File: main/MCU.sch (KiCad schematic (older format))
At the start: 22 parts, among them J10 MCU_debug, J11 MCU_GPIO, J12 Conn_02x04_Odd_Even, U5 EFM32GG12B810F1024GQ64, X2 MCU Oscillator (72MHZ)

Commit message: Fix up after review 3
Add +3.3V and GND to MCU and FPGA GPIO.

Add a lot of footprints.
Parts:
- removed J11: MCU_GPIO, symbol Connector_Generic:Conn_02x05_Counter_Clockwise
- added J5: MCU_GPIO, symbol Connector_Generic:Conn_02x06_Odd_Even
- J12: value Conn_02x04_Odd_Even -> BACKUP_SPI
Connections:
- wire segments 177 -> 181
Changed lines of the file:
@@
 $Descr A4 11693 8268
 encoding utf-8
-Sheet 7 7
+Sheet 6 7
 Title "MIDI Audio Box"
 Date "2021-09-21"
@@
 Text Notes 3950 6850 0    50   ~ 10
 Decoupling capacitors (see AN0002.1, page 13)
-$Comp
-L Connector_Generic:Conn_02x05_Counter_Clockwise J11
-U 1 1 6149651E
-P 1500 4800
-F 0 "J11" H 1550 5217 50  0000 C CNN
-F 1 "MCU_GPIO" H 1550 5126 50  0000 C CNN
-F 2 "" H 1500 4800 50  0001 C CNN
-F 3 "~" H 1500 4800 50  0001 C CNN
-	1    1500 4800
-	1    0    0    -1
-$EndComp
 Wire Bus Line
-	900  5150 2200 5150
+	900  5700 2200 5700
 Wire Bus Line
 	2200 4450 4150 4450
@@
 P 1100 6500
 F 0 "J12" H 1150 6075 50  0000 C CNN
-F 1 "Conn_02x04_Odd_Even" H 1150 6166 50  0000 C CNN
+F 1 "BACKUP_SPI" H 1150 6166 50  0000 C CNN
 F 2 "" H 1100 6500 50  0001 C CNN
 F 3 "~" H 1100 6500 50  0001 C CNN
@@
 High Frequency Oscillator
 NoConn ~ 4650 4950
+$Comp
+L Connector_Generic:Conn_02x06_Odd_Even J5
+U 1 1 61CACD05
+P 1500 4800
+F 0 "J5" H 1550 5217 50  0000 C CNN
+F 1 "MCU_GPIO" H 1550 5126 50  0000 C CNN
+F 2 "" H 1500 4800 50  0001 C CNN
+F 3 "~" H 1500 4800 50  0001 C CNN
+	1    1500 4800
+	1    0    0    -1
+$EndComp
+$Comp
+L power:+3.3V #PWR076
+U 1 1 61CC3716
+P 1200 5250
+F 0 "#PWR076" H 1200 5100 50  0001 C CNN
+F 1 "+3.3V" H 1215 5423 50  0000 C CNN
+F 2 "" H 1200 5250 50  0001 C CNN
+F 3 "" H 1200 5250 50  0001 C CNN
+	1    1200 5250
+	-1   0    0    1
+$EndComp
+Wire Wire Line
+	1200 5250 1200 5100
+Wire Wire Line
+	1200 5100 1300 5100
+$Comp
+L power:GND #PWR077
+U 1 1 61CCF946
+P 1950 5300
+F 0 "#PWR077" H 1950 5050 50  0001 C CNN
+F 1 "GND" H 1955 5127 50  0000 C CNN
+F 2 "" H 1950 5300 50  0001 C CNN
+F 3 "" H 1950 5300 50  0001 C CNN
+	1    1950 5300
+	1    0    0    -1
+$EndComp
+Wire Wire Line
+	1950 5300 1950 5100
+Wire Wire Line
+	1950 5100 1800 5100
 Wire Bus Line
 	5250 950  5250 1650
 Wire Bus Line
-	2200 4450 2200 5150
+	2200 4450 2200 5700
 Wire Bus Line
-	900  4700 900  5150
+	900  4700 900  5700
 Wire Bus Line
 	4150 3450 4150 4450

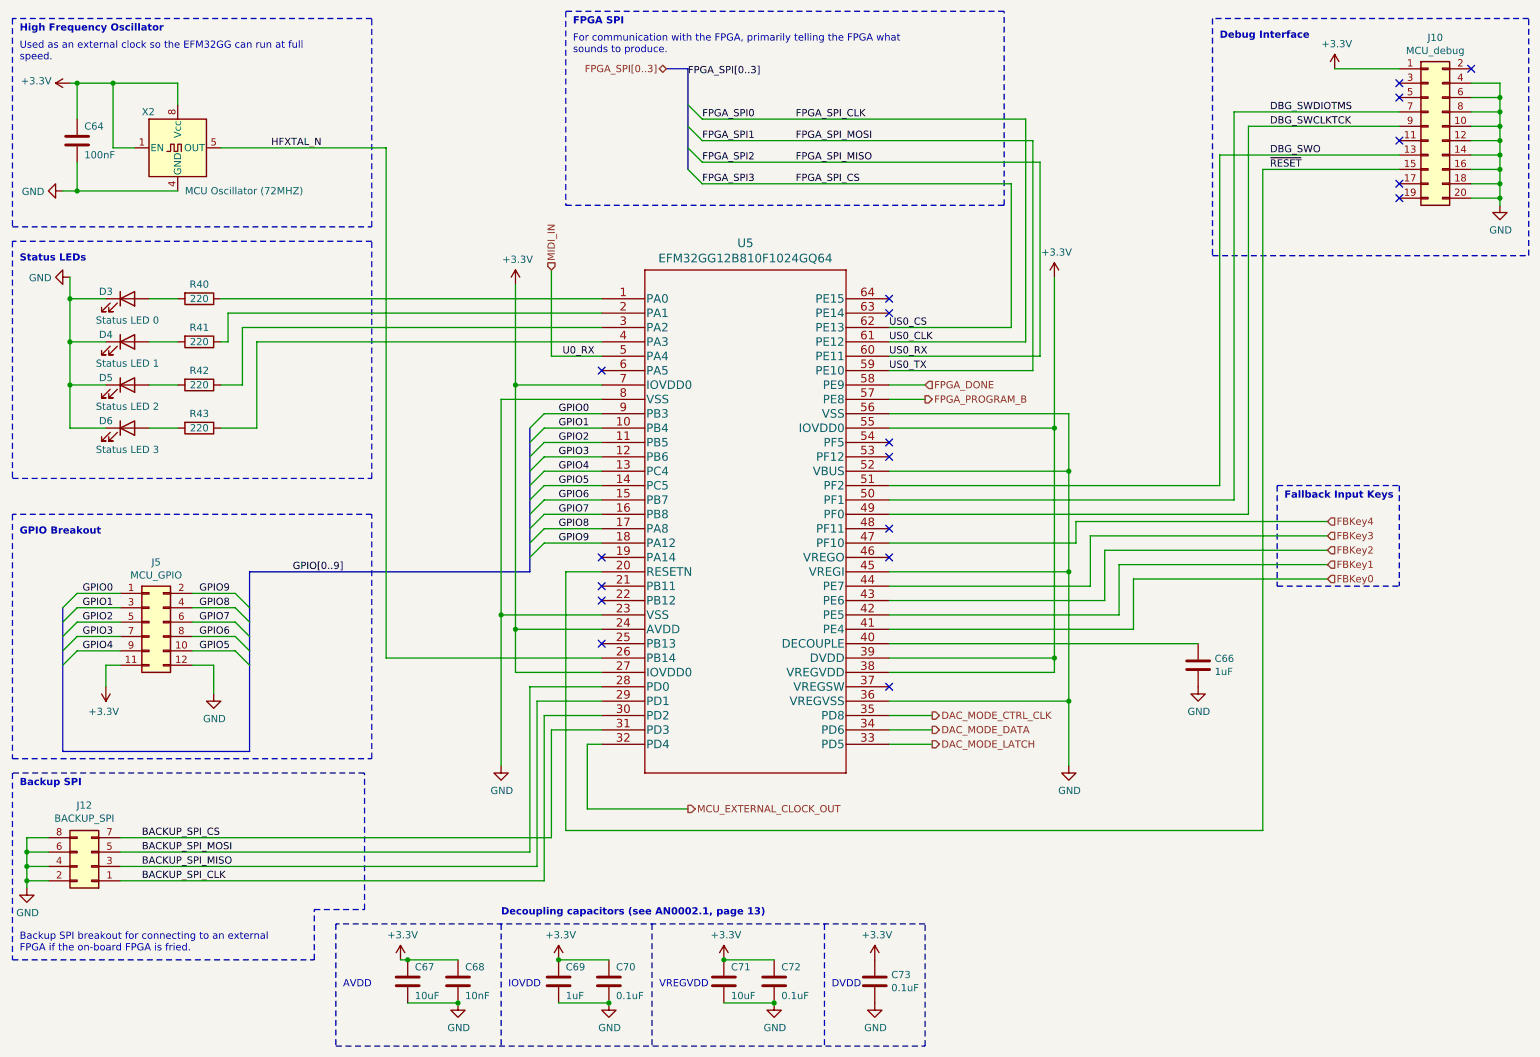
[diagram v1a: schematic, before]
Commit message: DAC: Remove amplifier, replace with low pass as per datasheet
Also: a lot of footprint association
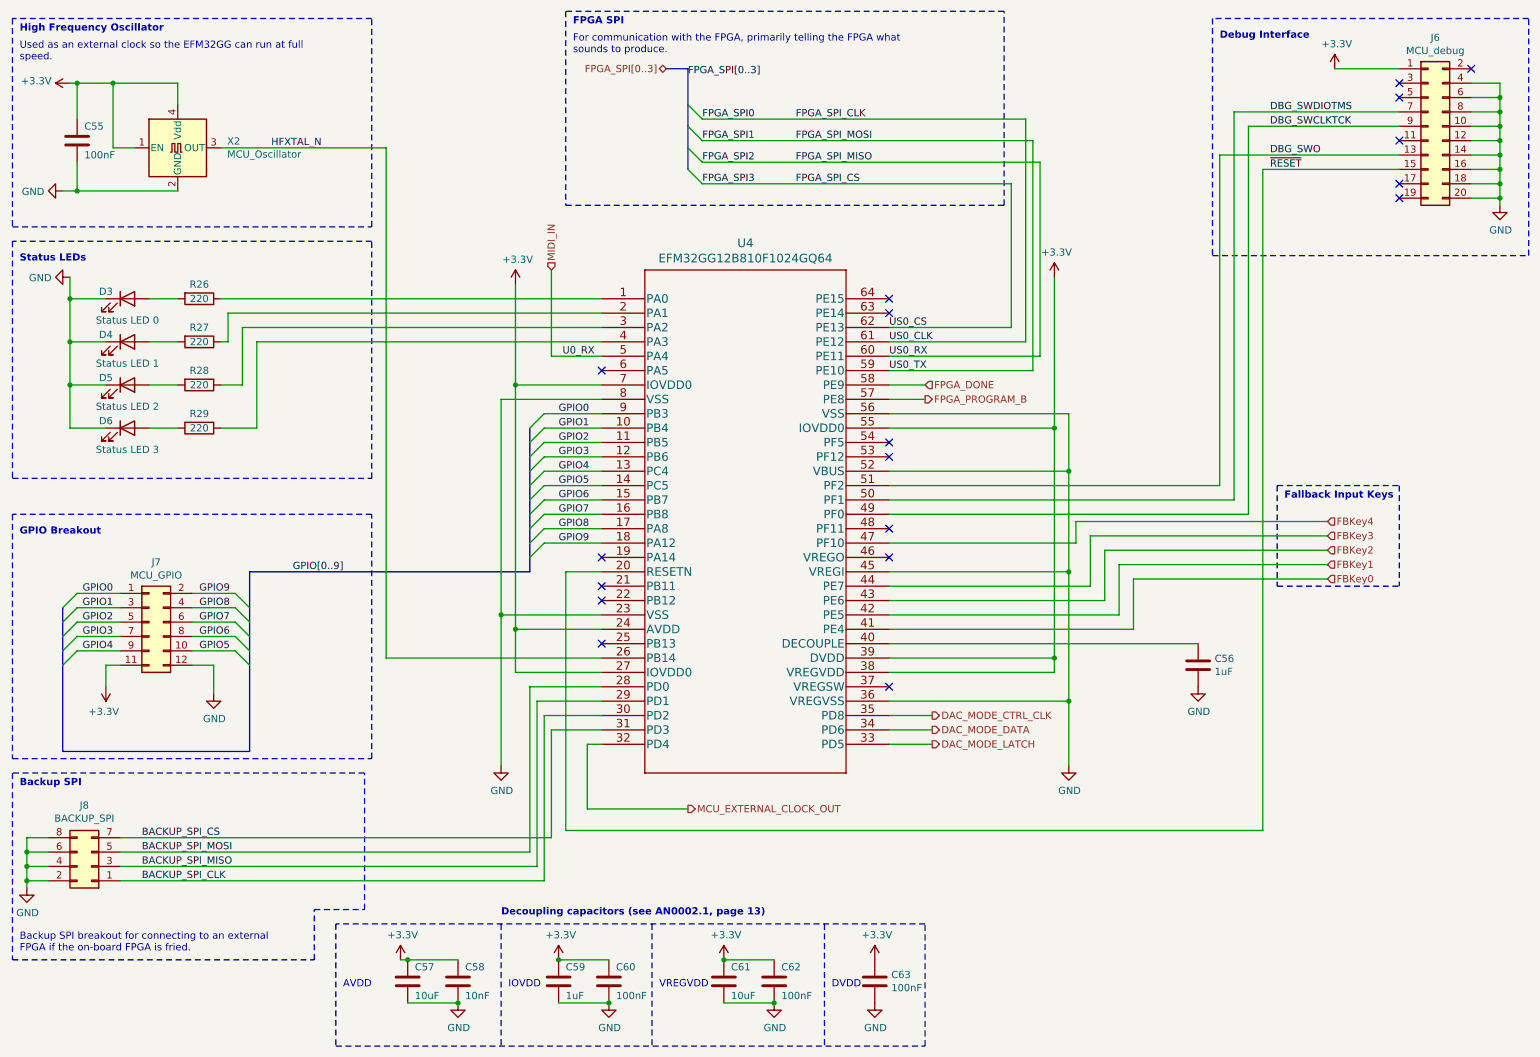
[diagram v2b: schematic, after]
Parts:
- removed X2: MCU Oscillator (72MHZ), Oscillator:Oscillator_DIP-8, symbol Oscillator:CXO_DIP8
- added X2: MCU_Oscillator, symbol Oscillator:TXC-7C
- C55: renamed from C64; footprint (none) -> Capacitor_SMD:C_0805_2012Metric_Pad1.18x1.45mm_HandSolder
- C56: renamed from C66; footprint (none) -> Capacitor_SMD:C_0805_2012Metric_Pad1.18x1.45mm_HandSolder
- C57: renamed from C67; footprint (none) -> Capacitor_SMD:C_0805_2012Metric_Pad1.18x1.45mm_HandSolder
- C58: renamed from C68; footprint (none) -> Capacitor_SMD:C_0805_2012Metric_Pad1.18x1.45mm_HandSolder
- C59: renamed from C69; footprint (none) -> Capacitor_SMD:C_0805_2012Metric_Pad1.18x1.45mm_HandSolder
- C60: renamed from C70; value 0.1uF -> 100nF; footprint (none) -> Capacitor_SMD:C_0805_2012Metric_Pad1.18x1.45mm_HandSolder
- C61: renamed from C71; footprint (none) -> Capacitor_SMD:C_0805_2012Metric_Pad1.18x1.45mm_HandSolder
- C62: renamed from C72; value 0.1uF -> 100nF; footprint (none) -> Capacitor_SMD:C_0805_2012Metric_Pad1.18x1.45mm_HandSolder
- C63: renamed from C73; value 0.1uF -> 100nF; footprint (none) -> Capacitor_SMD:C_0805_2012Metric_Pad1.18x1.45mm_HandSolder
- J6: renamed from J10; footprint (none) -> Connector_PinHeader_1.27mm:PinHeader_2x10_P1.27mm_Vertical
- J7: renamed from J5; footprint (none) -> Connector_PinHeader_2.54mm:PinHeader_2x06_P2.54mm_Vertical
- J8: renamed from J12; footprint (none) -> Connector_PinHeader_2.54mm:PinHeader_2x04_P2.54mm_Vertical
- renumbered R40 to R26, R41 to R27, R42 to R28, R43 to R29, U5 to U4
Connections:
- net +3V3: now also X2.1 (EN), X2.4 (Vdd)
- net GND: now also X2.2 (GND)
- net HFXTAL_N: now also X2.3 (OUT)

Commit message: Start PCB layout
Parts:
- D3: value Status LED 0 -> Status LED; Manufacturer_Name (none) -> Wurth Electronic; Manufacturer_Part_Number (none) -> 150080RS75000; URL (none) -> https://no.farnell.com/wurth-elektronik/150080rs75000/led-0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
- D4: value Status LED 1 -> Status LED; Manufacturer_Name (none) -> Wurth Electronic; Manufacturer_Part_Number (none) -> 150080RS75000; URL (none) -> https://no.farnell.com/wurth-elektronik/150080rs75000/led-0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
- D5: value Status LED 2 -> Status LED; Manufacturer_Name (none) -> Wurth Electronic; Manufacturer_Part_Number (none) -> 150080RS75000; URL (none) -> https://no.farnell.com/wurth-elektronik/150080rs75000/led-0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
- D6: value Status LED 3 -> Status LED; Manufacturer_Name (none) -> Wurth Electronic; Manufacturer_Part_Number (none) -> 150080RS75000; URL (none) -> https://no.farnell.com/wurth-elektronik/150080rs75000/led-0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
- J7, J8: Comment (none) -> Same as FPGA_GPIO (Cut to length)
- U4: Manufacturer_Name (none) -> Silicon Labs; Manufacturer_Part_Number (none) -> EFM32GG12B810F1024GQ64-A; URL (none) -> https://no.farnell.com/silicon-labs/efm32gg12b810f1024gq64-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
- X2: footprint (none) -> Oscillator:Oscillator_SMD_SeikoEpson_SG210-4Pin_2.5x2.0mm_HandSoldering
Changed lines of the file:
@@
 F 1 "EFM32GG12B810F1024GQ64" H 5650 2831 60  0000 C CNN
 F 2 "EFM32GG12B810F1024Q64:EFM32GG12B810F1024GQ64" H 5650 2790 60  0001 C CNN
-F 3 "" H 4650 2550 60  0000 C CNN
+F 3 "https://www.farnell.com/datasheets/2719978.pdf" H 4650 2550 60  0000 C CNN
+F 4 "Silicon Labs" H 4650 2550 50  0001 C CNN "Manufacturer_Name"
+F 5 "EFM32GG12B810F1024GQ64-A" H 4650 2550 50  0001 C CNN "Manufacturer_Part_Number"
+F 6 "https://no.farnell.com/silicon-labs/efm32gg12b810f1024gq64-a/mcu-32bit-72mhz-qfp-64/dp/2950057" H 4650 2550 50  0001 C CNN "URL"
 	1    4650 2550
 	1    0    0    -1
@@
 P 1350 3450
 F 0 "D6" H 1200 3500 50  0000 C CNN
-F 1 "Status LED 3" H 1350 3300 50  0000 C CNN
+F 1 "Status LED" H 1350 3300 50  0000 C CNN
 F 2 "LED_SMD:LED_0805_2012Metric_Pad1.15x1.40mm_HandSolder" H 1350 3450 50  0001 C CNN
-F 3 "~" H 1350 3450 50  0001 C CNN
+F 3 "https://www.farnell.com/datasheets/1911350.pdf" H 1350 3450 50  0001 C CNN
+F 4 "Wurth Electronic" H 1350 3450 50  0001 C CNN "Manufacturer_Name"
+F 5 "150080RS75000" H 1350 3450 50  0001 C CNN "Manufacturer_Part_Number"
+F 6 "https://no.farnell.com/wurth-elektronik/150080rs75000/led-0805-red-150mcd-625nm/dp/2322077?st=0805%20led" H 1350 3450 50  0001 C CNN "URL"
 	1    1350 3450
 	1    0    0    -1
@@
 P 1350 3150
 F 0 "D5" H 1200 3200 50  0000 C CNN
-F 1 "Status LED 2" H 1350 3000 50  0000 C CNN
+F 1 "Status LED" H 1350 3000 50  0000 C CNN
 F 2 "LED_SMD:LED_0805_2012Metric_Pad1.15x1.40mm_HandSolder" H 1350 3150 50  0001 C CNN
-F 3 "~" H 1350 3150 50  0001 C CNN
+F 3 "https://www.farnell.com/datasheets/1911350.pdf" H 1350 3150 50  0001 C CNN
+F 4 "Wurth Electronic" H 1350 3150 50  0001 C CNN "Manufacturer_Name"
+F 5 "150080RS75000" H 1350 3150 50  0001 C CNN "Manufacturer_Part_Number"
+F 6 "https://no.farnell.com/wurth-elektronik/150080rs75000/led-0805-red-150mcd-625nm/dp/2322077?st=0805%20led" H 1350 3150 50  0001 C CNN "URL"
 	1    1350 3150
 	1    0    0    -1
@@
 P 1350 2850
 F 0 "D4" H 1200 2900 50  0000 C CNN
-F 1 "Status LED 1" H 1350 2700 50  0000 C CNN
+F 1 "Status LED" H 1350 2700 50  0000 C CNN
 F 2 "LED_SMD:LED_0805_2012Metric_Pad1.15x1.40mm_HandSolder" H 1350 2850 50  0001 C CNN
-F 3 "~" H 1350 2850 50  0001 C CNN
+F 3 "https://www.farnell.com/datasheets/1911350.pdf" H 1350 2850 50  0001 C CNN
+F 4 "Wurth Electronic" H 1350 2850 50  0001 C CNN "Manufacturer_Name"
+F 5 "150080RS75000" H 1350 2850 50  0001 C CNN "Manufacturer_Part_Number"
+F 6 "https://no.farnell.com/wurth-elektronik/150080rs75000/led-0805-red-150mcd-625nm/dp/2322077?st=0805%20led" H 1350 2850 50  0001 C CNN "URL"
 	1    1350 2850
 	1    0    0    -1
@@
 P 1350 2550
 F 0 "D3" H 1200 2600 50  0000 C CNN
-F 1 "Status LED 0" H 1350 2400 50  0000 C CNN
+F 1 "Status LED" H 1350 2400 50  0000 C CNN
 F 2 "LED_SMD:LED_0805_2012Metric_Pad1.15x1.40mm_HandSolder" H 1350 2550 50  0001 C CNN
-F 3 "~" H 1350 2550 50  0001 C CNN
+F 3 "https://www.farnell.com/datasheets/1911350.pdf" H 1350 2550 50  0001 C CNN
+F 4 "Wurth Electronic" H 1350 2550 50  0001 C CNN "Manufacturer_Name"
+F 5 "150080RS75000" H 1350 2550 50  0001 C CNN "Manufacturer_Part_Number"
+F 6 "https://no.farnell.com/wurth-elektronik/150080rs75000/led-0805-red-150mcd-625nm/dp/2322077?st=0805%20led" H 1350 2550 50  0001 C CNN "URL"
 	1    1350 2550
 	1    0    0    -1
@@
 F 2 "Connector_PinHeader_2.54mm:PinHeader_2x04_P2.54mm_Vertical" H 1100 6500 50  0001 C CNN
 F 3 "~" H 1100 6500 50  0001 C CNN
+F 4 "Same as FPGA_GPIO (Cut to length)" H 1100 6500 50  0001 C CNN "Comment"
 	1    1100 6500
 	-1   0    0    1
@@
 F 2 "Connector_PinHeader_2.54mm:PinHeader_2x06_P2.54mm_Vertical" H 1500 4800 50  0001 C CNN
 F 3 "~" H 1500 4800 50  0001 C CNN
+F 4 "Same as FPGA_GPIO (Cut to length)" H 1500 4800 50  0001 C CNN "Comment"
 	1    1500 4800
 	1    0    0    -1
@@
 F 0 "X2" H 2044 1546 50  0000 L CNN
 F 1 "MCU_Oscillator" H 2044 1455 50  0000 L CNN
-F 2 "" H 2400 1150 50  0001 C CNN
+F 2 "Oscillator:Oscillator_SMD_SeikoEpson_SG210-4Pin_2.5x2.0mm_HandSoldering" H 2400 1150 50  0001 C CNN
 F 3 "http://www.txccorp.com/download/products/osc/7C_o.pdf" H 1600 1500 50  0001 C CNN
 	1    1700 1500
